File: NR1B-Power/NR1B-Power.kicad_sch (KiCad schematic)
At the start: 43 parts, among them J1 Conn_02x04_Odd_Even, J2 Conn_02x04_Odd_Even, J3 3.81mm Pluggable Terminal, U1 TSR_1-2450, U2 DKMW06, U3 VO615A, U4 VO615A, X1 NUCLEO144-ZIO

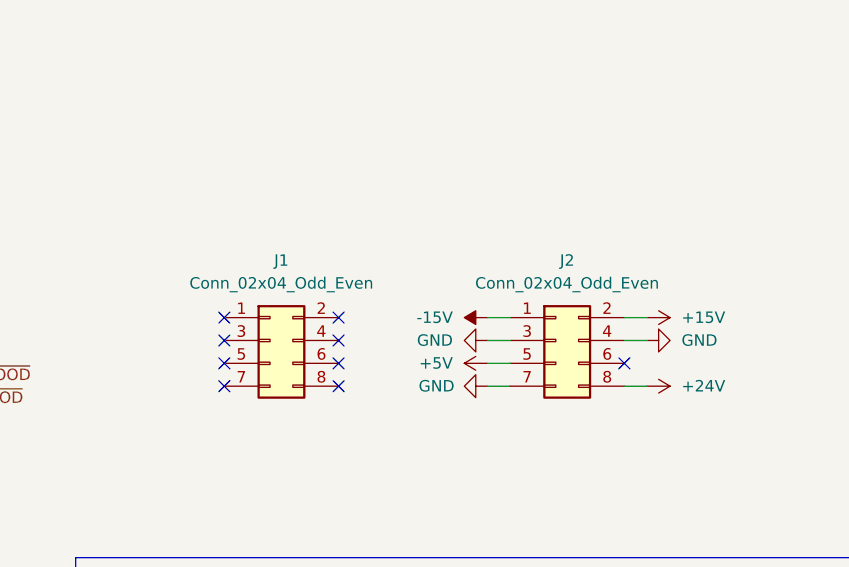
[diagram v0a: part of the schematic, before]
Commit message: Added Manufacturers and part numbers
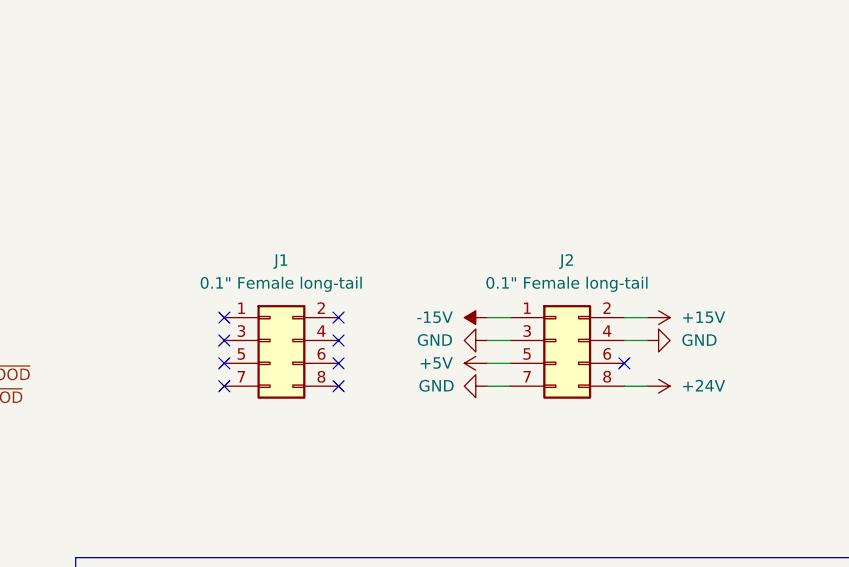
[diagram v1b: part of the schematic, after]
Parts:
- D7, D8: MPN APT2012LZGCK -> APT2012LSECK/J3-PRV
- F3: MFG 1 (none) -> Bel Fuse; MPN 1 (none) -> 0ZCG0030FF2C
- J1, J2: value Conn_02x04_Odd_Even -> 0.1" Female long-tail; MFG 1 (none) -> Mill-Max; MPN 1 (none) -> 411-XX-2XX-41-001000
- J3: MFG 1 (none) -> CUI; MPN 1 (none) -> TBP03R1-350-02BE
- U1: MFG 1 (none) -> TRACO; MPN 1 (none) -> TSR 1-2450
- U2: MFG 1 (none) -> Mean Well; MPN 1 (none) -> DKMW06F-15
- U3, U4: MFG 1 (none) -> Vishay; MPN 1 (none) -> VO615A
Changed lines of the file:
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@@
+      (effects (font (size 1.27 1.27)) hide)
+    )
+    (property "MFG 1" "Mean Well" (id 4) (at 363.22 82.55 0)
+      (effects (font (size 1.27 1.27)) hide)
+    )
+    (property "MPN 1" "DKMW06F-15" (id 5) (at 363.22 82.55 0)
       (effects (font (size 1.27 1.27)) hide)
     )
@@
       (effects (font (size 1.27 1.27)) hide)
     )
+    (property "MFG 1" "TRACO" (id 4) (at 363.22 43.18 0)
+      (effects (font (size 1.27 1.27)) hide)
+    )
+    (property "MPN 1" "TSR 1-2450" (id 5) (at 363.22 43.18 0)
+      (effects (font (size 1.27 1.27)) hide)
+    )
     (pin "1")
     (pin "2")
@@
     (in_bom yes) (on_board yes) (fields_autoplaced)
     (property "Reference" "J2" (id 0) (at 189.23 46.99 0))
-    (property "Value" "Conn_02x04_Odd_Even" (id 1) (at 189.23 49.53 0))
+    (property "Value" "0.1\" Female long-tail" (id 1) (at 189.23 49.53 0))
     (property "Footprint" "Connector_PinHeader_2.54mm:PinHeader_2x04_P2.54mm_Vertical" (id 2) (at 187.96 55.88 0)
       (effects (font (size 1.27 1.27)) hide)
     )
     (property "Datasheet" "~" (id 3) (at 187.96 55.88 0)
+      (effects (font (size 1.27 1.27)) hide)
+    )
+    (property "MFG 1" "Mill-Max" (id 4) (at 187.96 55.88 0)
+      (effects (font (size 1.27 1.27)) hide)
+    )
+    (property "MPN 1" "411-XX-2XX-41-001000" (id 5) (at 187.96 55.88 0)
       (effects (font (size 1.27 1.27)) hide)
     )
@@
     )
     (property "Datasheet" "~" (id 3) (at 273.05 40.64 0)
+      (effects (font (size 1.27 1.27)) hide)
+    )
+    (property "MFG 1" "CUI" (id 4) (at 273.05 40.64 0)
+      (effects (font (size 1.27 1.27)) hide)
+    )
+    (property "MPN 1" "TBP03R1-350-02BE" (id 5) (at 273.05 40.64 0)
       (effects (font (size 1.27 1.27)) hide)
     )
@@
       (effects (font (size 1.27 1.27)) hide)
     )
-    (property "MPN" "APT2012LZGCK" (id 4) (at 342.9 30.48 90)
+    (property "MPN" "APT2012LSECK/J3-PRV" (id 4) (at 342.9 30.48 90)
       (effects (font (size 1.27 1.27)) hide)
     )
@@
       (effects (font (size 1.27 1.27)) hide)
     )
+    (property "MFG 1" "Vishay" (id 4) (at 284.48 148.59 0)
+      (effects (font (size 1.27 1.27)) hide)
+    )
+    (property "MPN 1" "VO615A" (id 5) (at 284.48 148.59 0)
+      (effects (font (size 1.27 1.27)) hide)
+    )
     (pin "1")
     (pin "2")
@@
     )
     (property "Datasheet" "http://www.vishay.com/docs/81753/vo615a.pdf" (id 3) (at 341.63 148.59 0)
+      (effects (font (size 1.27 1.27)) hide)
+    )
+    (property "MFG 1" "Vishay" (id 5) (at 341.63 148.59 0)
+      (effects (font (size 1.27 1.27)) hide)
+    )
+    (property "MPN 1" "VO615A" (id 4) (at 341.63 148.59 0)
       (effects (font (size 1.27 1.27)) hide)
     )
@@
       (effects (font (size 1.27 1.27)) hide)
     )
-    (property "MPN" "APT2012LZGCK" (id 4) (at 342.9 68.58 90)
+    (property "MPN" "APT2012LSECK/J3-PRV" (id 4) (at 342.9 68.58 90)
       (effects (font (size 1.27 1.27)) hide)
     )
@@
     (in_bom yes) (on_board yes) (fields_autoplaced)
     (property "Reference" "J1" (id 0) (at 157.48 46.99 0))
-    (property "Value" "Conn_02x04_Odd_Even" (id 1) (at 157.48 49.53 0))
+    (property "Value" "0.1\" Female long-tail" (id 1) (at 157.48 49.53 0))
     (property "Footprint" "Connector_PinHeader_2.54mm:PinHeader_2x04_P2.54mm_Vertical" (id 2) (at 156.21 55.88 0)
       (effects (font (size 1.27 1.27)) hide)
     )
     (property "Datasheet" "~" (id 3) (at 156.21 55.88 0)
+      (effects (font (size 1.27 1.27)) hide)
+    )
+    (property "MFG 1" "Mill-Max" (id 4) (at 156.21 55.88 0)
+      (effects (font (size 1.27 1.27)) hide)
+    )
+    (property "MPN 1" "411-XX-2XX-41-001000" (id 5) (at 156.21 55.88 0)
       (effects (font (size 1.27 1.27)) hide)
     )
@@
       (effects (font (size 1.27 1.27)) (justify left) hide)
     )
-    (property "Datasheet" "~" (id 3) (at 342.9 78.74 0)
+    (property "Datasheet" "https://belfuse.com/resources/datasheets/circuitprotection/ds-cp-0zcg-series.pdf" (id 3) (at 342.9 78.74 0)
+      (effects (font (size 1.27 1.27)) hide)
+    )
+    (property "MFG 1" "Bel Fuse" (id 4) (at 342.9 78.74 90)
+      (effects (font (size 1.27 1.27)) hide)
+    )
+    (property "MPN 1" "0ZCG0030FF2C" (id 5) (at 342.9 78.74 90)
       (effects (font (size 1.27 1.27)) hide)
     )
@@
     )
     (path "/c17ae2ea-c320-4586-86b4-0b8496adc1a9"
-      (reference "J1") (unit 1) (value "Conn_02x04_Odd_Even") (footprint "Connector_PinHeader_2.54mm:PinHeader_2x04_P2.54mm_Vertical")
+      (reference "J1") (unit 1) (value "0.1\" Female long-tail") (footprint "Connector_PinHeader_2.54mm:PinHeader_2x04_P2.54mm_Vertical")
     )
     (path "/48e1a80a-7278-460b-b182-18809159e44a"
-      (reference "J2") (unit 1) (value "Conn_02x04_Odd_Even") (footprint "Connector_PinHeader_2.54mm:PinHeader_2x04_P2.54mm_Vertical")
+      (reference "J2") (unit 1) (value "0.1\" Female long-tail") (footprint "Connector_PinHeader_2.54mm:PinHeader_2x04_P2.54mm_Vertical")
     )
     (path "/62501f8b-3aa4-48b1-9649-0ee8cff6d88e"

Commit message: Changed C1
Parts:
- C1: value 47uF -> 47uF 50V; footprint Capacitor_SMD:CP_Elec_5x5.3 -> Capacitor_SMD:CP_Elec_6.3x7.7
- C2: value 47uF -> 47uF 16V
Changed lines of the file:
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@@
       (effects (font (size 1.27 1.27)) (justify left))
     )
-    (property "Value" "47uF" (id 1) (at 381 46.1009 0)
+    (property "Value" "47uF 16V" (id 1) (at 381 46.1009 0)
       (effects (font (size 1.27 1.27)) (justify left))
     )
@@
   )
   (symbol (lib_id "Device:C_Polarized") (at 316.23 45.72 0) (unit 1)
-    (in_bom yes) (on_board yes) (fields_autoplaced)
+    (in_bom yes) (on_board yes)
     (property "Reference" "C1" (id 0) (at 320.04 43.5609 0)
       (effects (font (size 1.27 1.27)) (justify left))
     )
-    (property "Value" "47uF" (id 1) (at 320.04 46.1009 0)
-      (effects (font (size 1.27 1.27)) (justify left))
-    )
-    (property "Footprint" "Capacitor_SMD:CP_Elec_5x5.3" (id 2) (at 317.1952 49.53 0)
+    (property "Value" "47uF 50V" (id 1) (at 316.23 48.26 0)
+      (effects (font (size 1.27 1.27)) (justify left))
+    )
+    (property "Footprint" "Capacitor_SMD:CP_Elec_6.3x7.7" (id 2) (at 317.1952 49.53 0)
       (effects (font (size 1.27 1.27)) hide)
     )
@@
     )
     (path "/26cdb40e-93e6-480c-b78d-5e076e8bc364"
-      (reference "C1") (unit 1) (value "47uF") (footprint "Capacitor_SMD:CP_Elec_5x5.3")
+      (reference "C1") (unit 1) (value "47uF 50V") (footprint "Capacitor_SMD:CP_Elec_6.3x7.7")
     )
     (path "/00b811f3-23be-4a13-ada5-b5886d4d3293"
-      (reference "C2") (unit 1) (value "47uF") (footprint "Capacitor_SMD:CP_Elec_5x5.3")
+      (reference "C2") (unit 1) (value "47uF 16V") (footprint "Capacitor_SMD:CP_Elec_5x5.3")
     )
     (path "/f547b173-ebfb-49d6-b66f-236b277af6f2"

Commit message: Fixed footprints
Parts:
- D1: footprint Diode_SMD:D_SOD-323 -> Diode_SMD:D_SMA
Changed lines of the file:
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@@
     (property "Reference" "D1" (id 0) (at 300.99 34.29 0))
     (property "Value" "S1G" (id 1) (at 300.99 36.83 0))
-    (property "Footprint" "Diode_SMD:D_SOD-323" (id 2) (at 300.99 40.64 0)
+    (property "Footprint" "Diode_SMD:D_SMA" (id 2) (at 300.99 40.64 0)
       (effects (font (size 1.27 1.27)) hide)
     )
@@
     )
     (path "/6cb2bfc9-0227-4263-8e6a-9aa61a5200fe"
-      (reference "D1") (unit 1) (value "S1G") (footprint "Diode_SMD:D_SOD-323")
+      (reference "D1") (unit 1) (value "S1G") (footprint "Diode_SMD:D_SMA")
     )
     (path "/b154b91e-d5b0-4b9b-9cee-835aeda364c8"

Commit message: BOM updates
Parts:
- F3: value 250 mA -> 300 mA
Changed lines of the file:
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@@
   (title_block
     (title "NISoC Readout 1 Power Board")
-    (date "2022-07-22")
+    (date "2022-07-27")
     (rev "1.0")
     (company "University of Dallas")
@@
     (in_bom yes) (on_board yes) (fields_autoplaced)
     (property "Reference" "F3" (id 0) (at 342.9 72.39 90))
-    (property "Value" "250 mA" (id 1) (at 342.9 74.93 90))
+    (property "Value" "300 mA" (id 1) (at 342.9 74.93 90))
     (property "Footprint" "Fuse:Fuse_1812_4532Metric" (id 2) (at 347.98 77.47 0)
       (effects (font (size 1.27 1.27)) (justify left) hide)
@@
     )
     (path "/ec0d2c98-8323-40ff-abf5-0ab52e148e8a"
-      (reference "F3") (unit 1) (value "250 mA") (footprint "Fuse:Fuse_1812_4532Metric")
+      (reference "F3") (unit 1) (value "300 mA") (footprint "Fuse:Fuse_1812_4532Metric")
     )
     (path "/c75138cf-95a9-494d-8d16-c9699b97d881"
